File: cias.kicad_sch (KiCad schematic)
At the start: 69 parts, among them CN13 KEYBOARD, CN6 SERIAL_DB25M, CN7 PARALLEL_DB25F, J90 DRIVE_SWITCHER, J99 HD_ACT, Q501 2N3904, Q502 2N3906, Q503 2N3906, Q504 2N3904, Q711 2N3904, U38 MC1488, U39 MC1489, U42 NE555, U7 VIA_8520, U8 VIA_8520

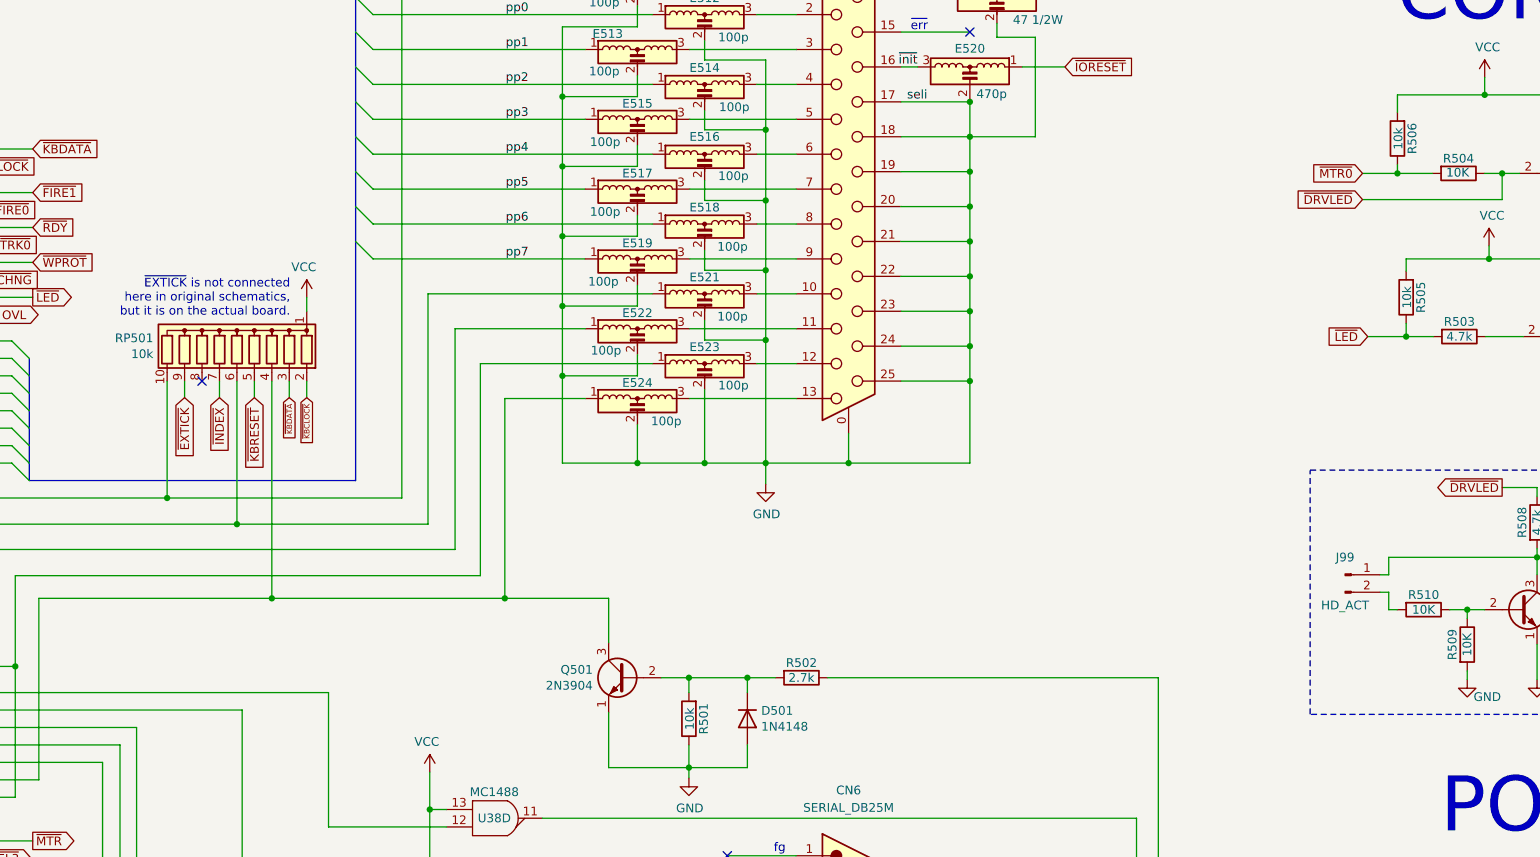
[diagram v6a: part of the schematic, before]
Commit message: Started cleaning up BOM
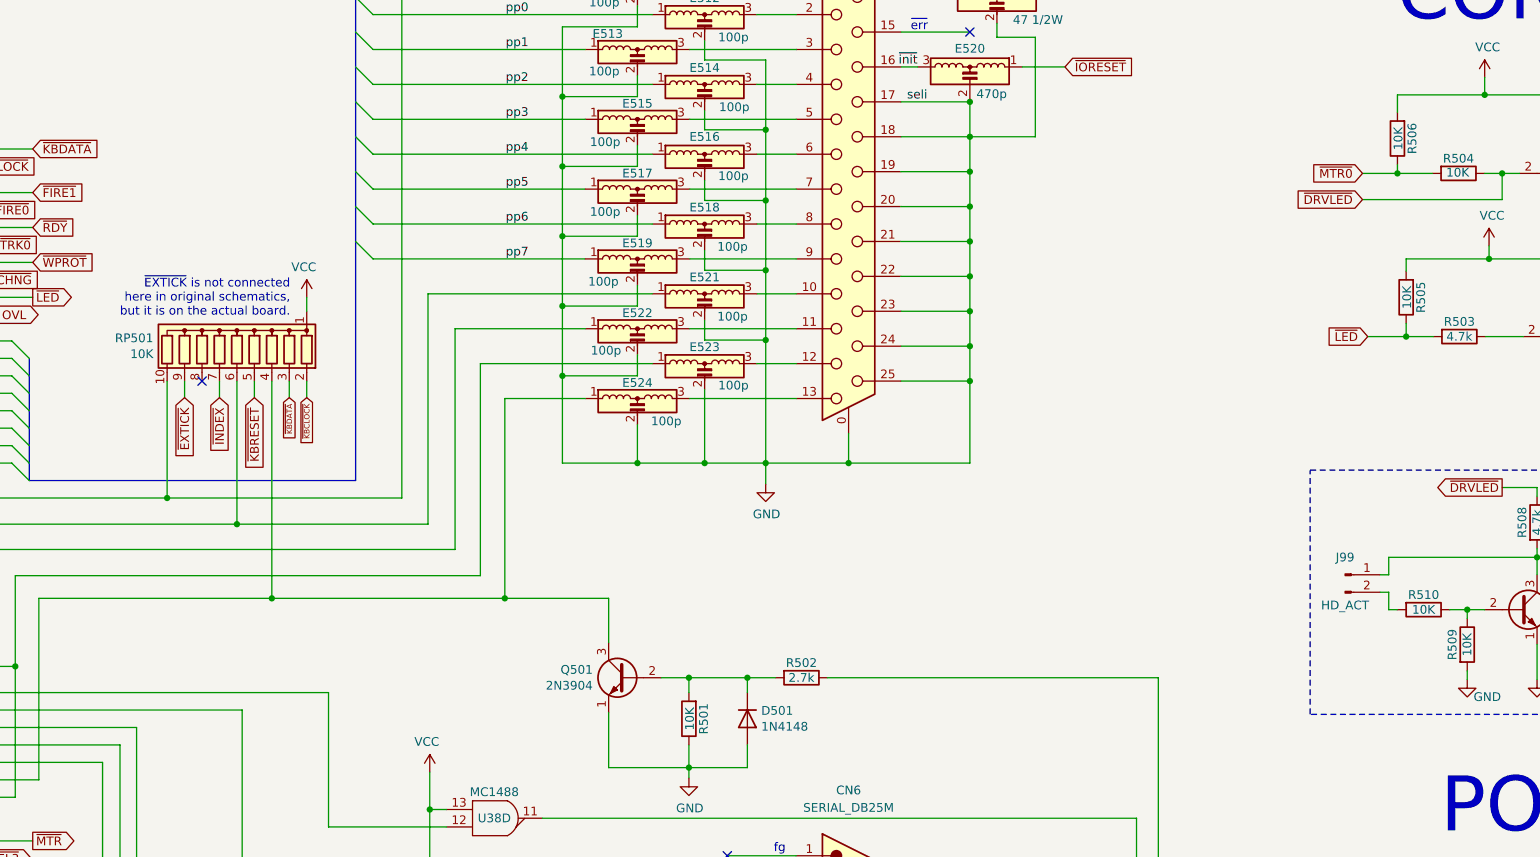
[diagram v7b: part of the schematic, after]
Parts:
- JP1, JP7B1: now left out of the parts list
- R501, R505, R506, RP501: value 10k -> 10K
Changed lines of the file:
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@@
 		(unit 1)
 		(exclude_from_sim no)
-		(in_bom yes)
+		(in_bom no)
 		(on_board yes)
 		(dnp no)
@@
 			)
 		)
-		(property "Value" "10k"
+		(property "Value" "10K"
 			(at 133.8834 89.789 0)
 			(effects
@@
 			)
 		)
-		(property "Value" "10k"
+		(property "Value" "10K"
 			(at 211.963 142.875 90)
 			(effects
@@
 			)
 		)
-		(property "Value" "10k"
+		(property "Value" "10K"
 			(at 315.087 58.42 90)
 			(effects
@@
 			)
 		)
-		(property "Value" "10k"
+		(property "Value" "10K"
 			(at 316.357 81.534 90)
 			(effects
@@
 		(unit 1)
 		(exclude_from_sim no)
-		(in_bom yes)
+		(in_bom no)
 		(on_board yes)
 		(dnp no)

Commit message: Working on BOM
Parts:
- C39, C7, C713, C8: MFG Part Num C410C103K1H5TAAUTO -> C410C103K1R5TA; Mouser (none) -> 80-C410C103K1R
- C42, C501, C502: MFG Part Num C412C334M5U5TA -> C440C334K5R5TA7200; Mouser (none) -> 80-C440C334K5R-TR
- C711: MFG Name AVX -> VISHAY; MFG Part Num SA115C104KAR -> A104K15X7RF5TAA; Mouser (none) -> 594-A104K15X7RF5TAA
- C712: MFG Part Num EEUFR1H100 -> ECA-1EM100I; Mouser (none) -> 667-ECA-1EM100I
- CN6: MFG Name (none) -> AMPHENOL; MFG Part Num (none) -> L717SDB25PA4CH4F; Mouser (none) -> 523-L717SDB25PA4CH4F
- CN7: MFG Name (none) -> AMPHENOL; MFG Part Num (none) -> L77SDB25SA4CH4F; Mouser (none) -> 523-L77SDB25SA4CH4F
- J90: now not fitted
